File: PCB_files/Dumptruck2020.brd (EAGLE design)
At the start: 35.6 x 59.1 mm, 16 parts, among them IC1 317EMP, Q1 N/A, Q2 N/A, Q3 N/A

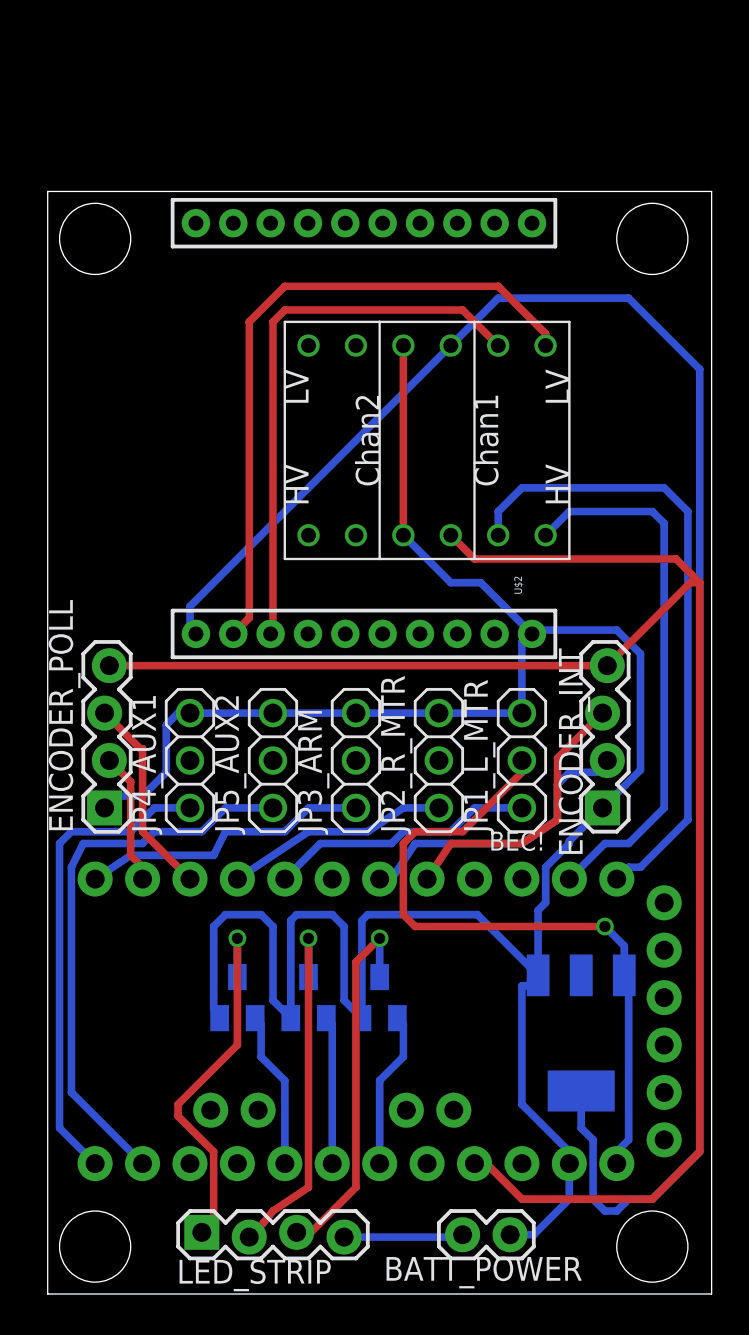
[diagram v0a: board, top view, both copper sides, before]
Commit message: Adding 2020 New PCB Files
This commit adds the new 2020 Eagle files for the
"Controls" board. Features a new switch.
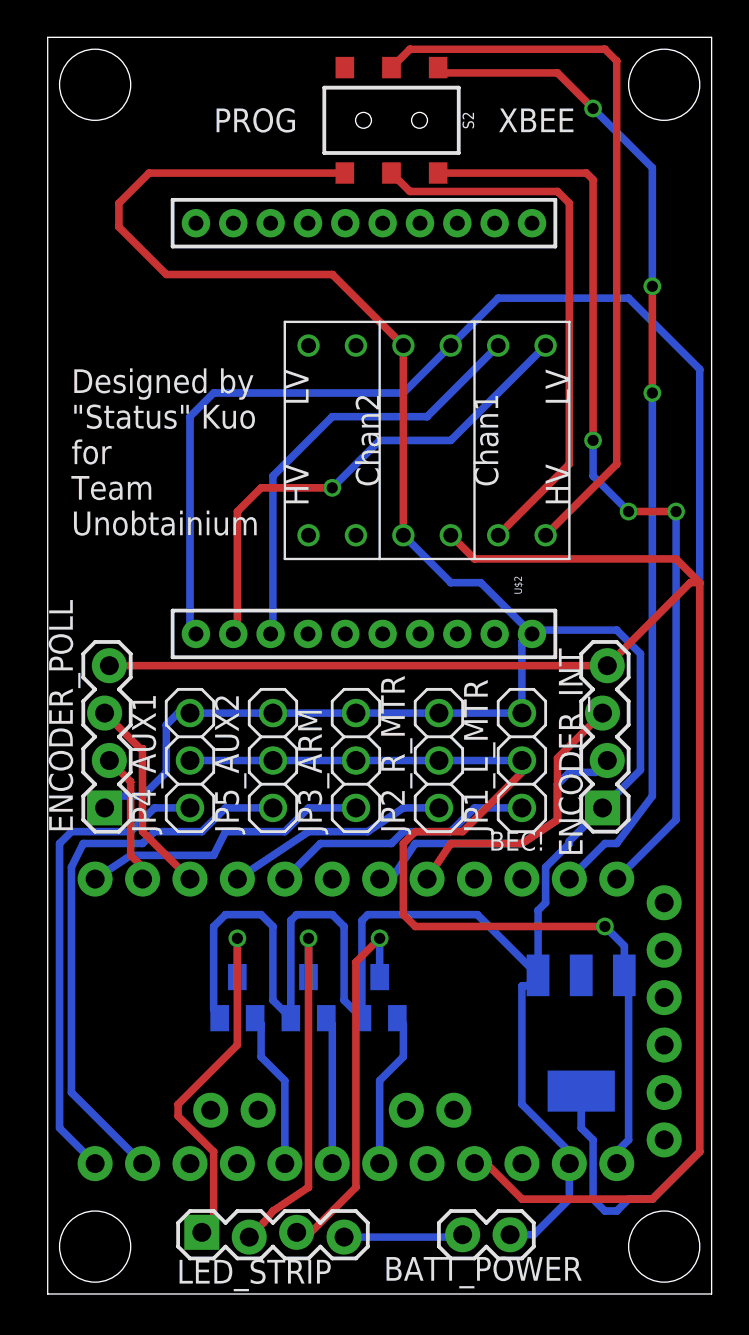
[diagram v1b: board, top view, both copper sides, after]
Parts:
- added S2: (no value), SparkFun-Switches:SWITCH_DPDT_SMD_AYZ0202
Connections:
- new net ARXO: S2.4, U$1.2
- new net ATXI: S2.1, U$1.1
- net ARXO_H: now also S2.5; no longer U$1.2
- net ATXI_H: now also S2.2; no longer U$1.1
- net GND: now also S2.3, S2.6
- net V+: now also JP2_R_MTR.2, JP3_ARM.2, JP4_AUX1.2, JP5_AUX2.2
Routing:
- net ARXO: track 0.00 -> 53.9 mm, vias 0 -> 3
- net ATXI: track 0.00 -> 50.5 mm, vias 0 -> 3
- net GND: track 137.9 -> 169.8 mm
- net V+: track 36.9 -> 54.6 mm
- net ARXO_H: track 29.0 -> 39.7 mm
- net ARXO_L: track 35.4 -> 26.8 mm, vias 0 -> 1
- net ATXI_L: track 29.9 -> 23.5 mm
- net +3V3: track 92.6 -> 98.5 mm
- net ATXI_H: track 34.1 -> 29.6 mm
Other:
- board size 35.6 x 59.1 mm -> 35.6 x 67.3 mm
- board text added: "Designed by "Status" Kuo for Team Unobtainium"
- board text added: "PROG"
- board text added: "XBEE"
